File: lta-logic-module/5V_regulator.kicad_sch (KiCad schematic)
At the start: 0 parts

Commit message: Full sketch of logic module schematic.
- Add button inputs
- Add LED signal driver / PWM combination
- Add 5V regulator based on LM2592
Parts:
- added C? (x2): (no value), symbol Device:C_Polarized_Small_US
- added D?: (no value), symbol Device:D_Schottky
- added L?: (no value), symbol Device:L_Small
- added R?: (no value), symbol Device:R_Small
- added U?: (no value), symbol Regulator_Switching:LM2595T-5
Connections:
- new net: R?.2, U?.5 (~{ON}/OFF)
- new net GND: C?.2, C?.2, D?.2 (A), R?.1, U?.3 (GND)
- new net VBATT: C?.1, U?.2 (VIN)
- new net VDD: C?.1, L?.1, U?.4 (FB)
- new net VOUT: D?.1 (K), L?.2, U?.1 (OUT)
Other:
- note added: "5V0 Buck Regulator - 1A max current"
- note added: "8--28Vin, 24V typ"
- note added: "Estimated power budget ---------------- MCU -- 25.0mA Button LEDs -- 180.0mA 74LVC244A -- 0.1mA 4x 74LVC00A -- 0.2mA 2x 74LVC14A -- 0.1mA 3x PCF8574 -- 0.3mA Pull-ups -- 0.1mA 16x FET driver inputs -- 25.0mA ------- 231mA"
- note added: "MPN: EST227M035AG4AA 35V low-ESR aluminum I_RMS > 250mA"
- note added: "MPN: TPSD686M020R0150 AVX TPS 20V low-ESR tantalum"
- note added: "Regulated 5V0 output"
- note added: "Target design load is 300mA"

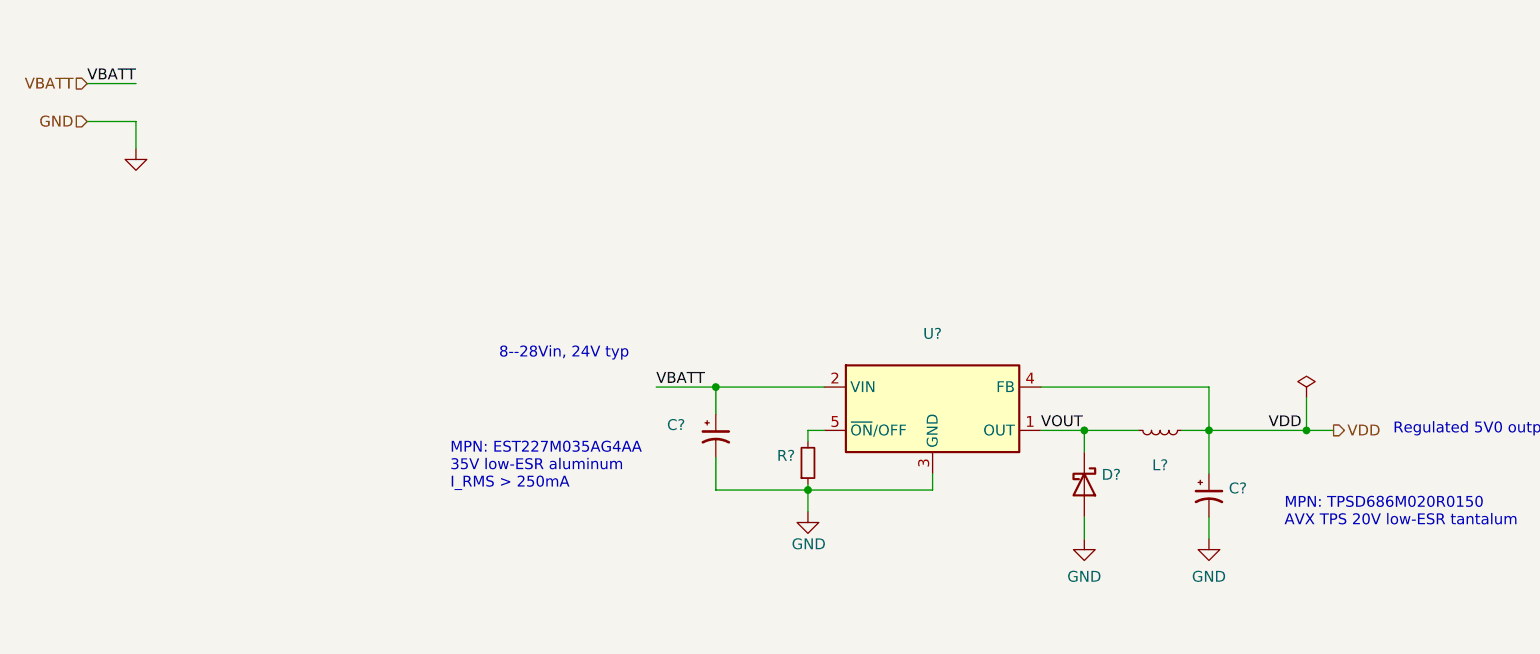
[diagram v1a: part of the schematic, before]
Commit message: Fix ERC violations.
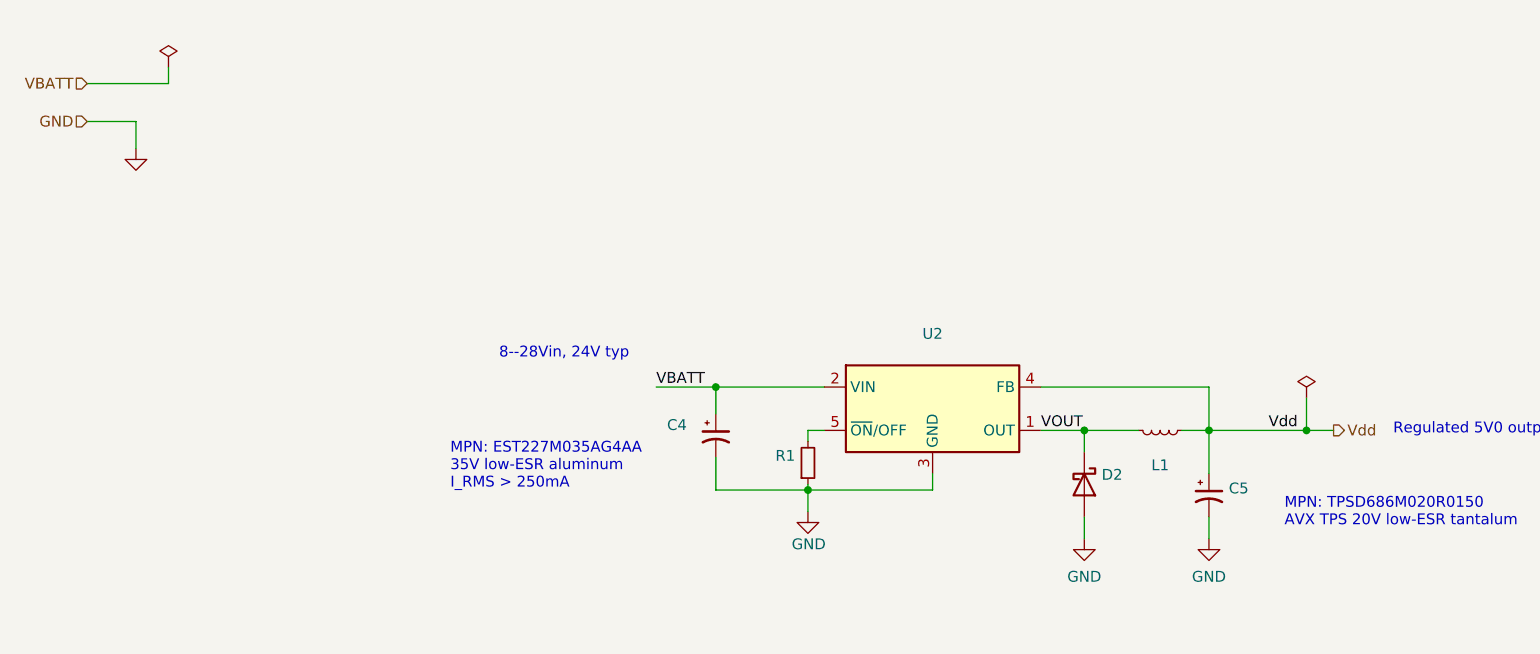
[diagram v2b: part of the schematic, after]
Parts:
- gave numbers to parts that had none: 6
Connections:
- net VDD renamed Vdd
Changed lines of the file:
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@@
+    (stroke (width 0) (type default) (color 0 0 0 0))
+  )
+  (wire (pts (xy 32.385 29.21) (xy 32.385 27.305))
     (stroke (width 0) (type default) (color 0 0 0 0))
   )
@@
     (stroke (width 0) (type default) (color 0 0 0 0))
   )
-  (wire (pts (xy 22.86 29.21) (xy 28.575 29.21))
+  (wire (pts (xy 22.86 29.21) (xy 32.385 29.21))
     (stroke (width 0) (type default) (color 0 0 0 0))
   )
@@
     (effects (font (size 1.27 1.27)) (justify left bottom))
   )
-  (label "VBATT" (at 28.575 29.21 180)
-    (effects (font (size 1.27 1.27)) (justify right bottom))
-  )
-  (label "VDD" (at 161.29 69.85 0)
+  (label "Vdd" (at 161.29 69.85 0)
     (effects (font (size 1.27 1.27)) (justify left bottom))
   )
@@
     (effects (font (size 1.27 1.27)) (justify right))
   )
-  (hierarchical_label "VDD" (shape output) (at 168.91 69.85 0)
+  (hierarchical_label "Vdd" (shape output) (at 168.91 69.85 0)
     (effects (font (size 1.27 1.27)) (justify left))
   )
   (symbol (lib_id "power:GND") (at 154.305 82.55 0) (unit 1)
     (in_bom yes) (on_board yes) (fields_autoplaced)
-    (property "Reference" "#PWR?" (id 0) (at 154.305 88.9 0)
+    (property "Reference" "#PWR020" (id 0) (at 154.305 88.9 0)
       (effects (font (size 1.27 1.27)) hide)
     )
@@
   (symbol (lib_id "Device:C_Polarized_Small_US") (at 96.52 70.485 0) (unit 1)
     (in_bom yes) (on_board yes)
-    (property "Reference" "C?" (id 0) (at 90.805 69.215 0)
+    (property "Reference" "C4" (id 0) (at 90.805 69.215 0)
       (effects (font (size 1.27 1.27)) (justify left))
     )
@@
   (symbol (lib_id "Device:R_Small") (at 107.315 73.66 0) (mirror x) (unit 1)
     (in_bom yes) (on_board yes) (fields_autoplaced)
-    (property "Reference" "R?" (id 0) (at 105.8165 72.8253 0)
+    (property "Reference" "R1" (id 0) (at 105.8165 72.8253 0)
       (effects (font (size 1.27 1.27)) (justify right))
     )
@@
   (symbol (lib_id "power:PWR_FLAG") (at 165.735 66.04 0) (unit 1)
     (in_bom yes) (on_board yes) (fields_autoplaced)
-    (property "Reference" "#FLG?" (id 0) (at 165.735 64.135 0)
+    (property "Reference" "#FLG03" (id 0) (at 165.735 64.135 0)
       (effects (font (size 1.27 1.27)) hide)
     )
@@
   (symbol (lib_id "Device:L_Small") (at 148.59 69.85 270) (unit 1)
     (in_bom yes) (on_board yes)
-    (property "Reference" "L?" (id 0) (at 148.59 73.9308 90))
+    (property "Reference" "L1" (id 0) (at 148.59 73.9308 90))
     (property "Value" "" (id 1) (at 148.59 71.755 90))
     (property "Footprint" "" (id 2) (at 148.59 69.85 0)
@@
   (symbol (lib_id "Device:D_Schottky") (at 139.7 76.2 270) (unit 1)
     (in_bom yes) (on_board yes) (fields_autoplaced)
-    (property "Reference" "D?" (id 0) (at 141.732 75.0478 90)
+    (property "Reference" "D2" (id 0) (at 141.732 75.0478 90)
       (effects (font (size 1.27 1.27)) (justify left))
     )
@@
   (symbol (lib_id "power:GND") (at 139.7 82.55 0) (unit 1)
     (in_bom yes) (on_board yes) (fields_autoplaced)
-    (property "Reference" "#PWR?" (id 0) (at 139.7 88.9 0)
+    (property "Reference" "#PWR019" (id 0) (at 139.7 88.9 0)
       (effects (font (size 1.27 1.27)) hide)
     )
@@
   (symbol (lib_id "power:GND") (at 28.575 36.83 0) (unit 1)
     (in_bom yes) (on_board yes) (fields_autoplaced)
-    (property "Reference" "#PWR?" (id 0) (at 28.575 43.18 0)
+    (property "Reference" "#PWR017" (id 0) (at 28.575 43.18 0)
       (effects (font (size 1.27 1.27)) hide)
     )
@@
   (symbol (lib_id "power:GND") (at 107.315 79.375 0) (unit 1)
     (in_bom yes) (on_board yes)
-    (property "Reference" "#PWR?" (id 0) (at 107.315 85.725 0)
+    (property "Reference" "#PWR018" (id 0) (at 107.315 85.725 0)
       (effects (font (size 1.27 1.27)) hide)
     )
@@
   (symbol (lib_id "Regulator_Switching:LM2595T-5") (at 121.92 67.31 0) (unit 1)
     (in_bom yes) (on_board yes) (fields_autoplaced)
-    (property "Reference" "U?" (id 0) (at 121.92 58.5302 0))
+    (property "Reference" "U2" (id 0) (at 121.92 58.5302 0))
     (property "Value" "" (id 1) (at 121.92 61.0671 0))
     (property "Footprint" "" (id 2) (at 123.19 73.66 0)
@@
   (symbol (lib_id "Device:C_Polarized_Small_US") (at 154.305 77.47 0) (unit 1)
     (in_bom yes) (on_board yes) (fields_autoplaced)
-    (property "Reference" "C?" (id 0) (at 156.6291 76.6416 0)
+    (property "Reference" "C5" (id 0) (at 156.6291 76.6416 0)
       (effects (font (size 1.27 1.27)) (justify left))
     )
@@
     (pin "2")
   )
+  (symbol (lib_id "power:PWR_FLAG") (at 32.385 27.305 0) (unit 1)
+    (in_bom yes) (on_board yes) (fields_autoplaced)
+    (property "Reference" "#FLG02" (id 0) (at 32.385 25.4 0)
+      (effects (font (size 1.27 1.27)) hide)
+    )
+    (property "Value" "" (id 1) (at 32.385 23.7292 0))
+    (property "Footprint" "" (id 2) (at 32.385 27.305 0)
+      (effects (font (size 1.27 1.27)) hide)
+    )
+    (property "Datasheet" "~" (id 3) (at 32.385 27.305 0)
+      (effects (font (size 1.27 1.27)) hide)
+    )
+    (pin "1")
+  )
 )

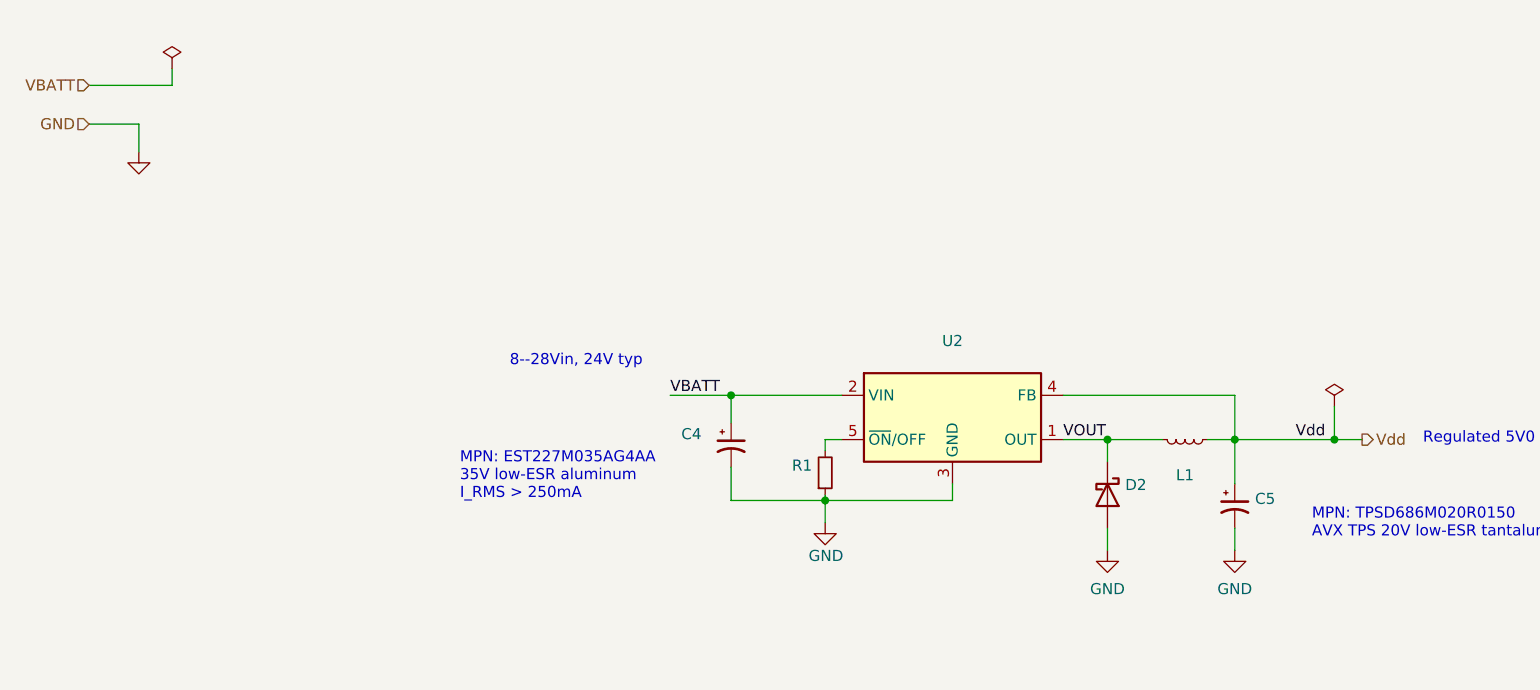
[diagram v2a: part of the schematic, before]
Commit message: Add TODOs, update some footprints.
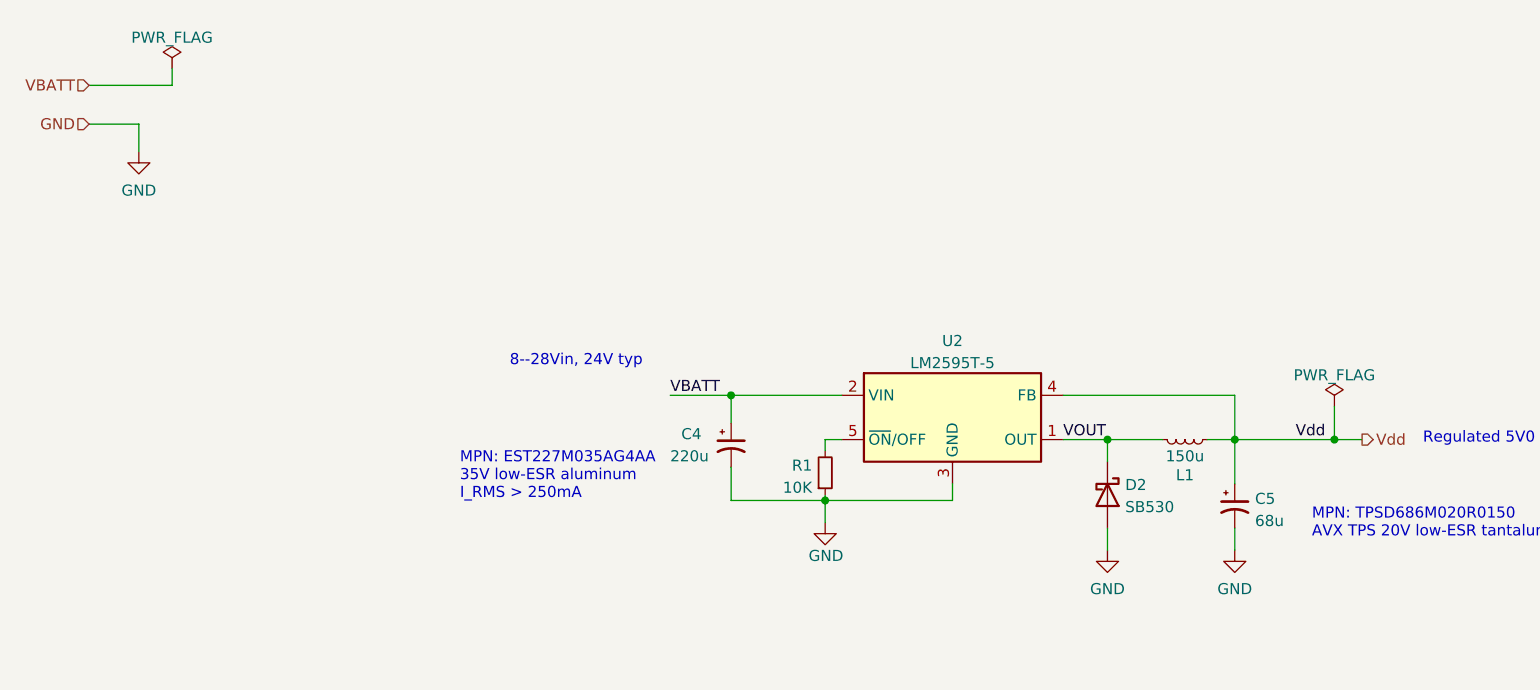
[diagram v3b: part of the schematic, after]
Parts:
- C4: value (none) -> 220u; footprint (none) -> Capacitor_THT:CP_Radial_D8.0mm_P3.50mm
- C5: value (none) -> 68u; footprint (none) -> Capacitor_Tantalum_SMD:CP_EIA-7343-30_AVX-N
- D2: value (none) -> SB530; footprint (none) -> Diode_THT:D_DO-201AD_P15.24mm_Horizontal
- L1: value (none) -> 150u; footprint (none) -> Aaron_THT:L_Radial_D13.5mm_P7.50mm
- R1: value (none) -> 10K; footprint (none) -> Resistor_SMD:R_0603_1608Metric; Comment (none) -> 10K 0603 resistor; +/-1%; 1/10W; MANUFACTURER (none) -> YAEGO; MPN (none) -> RC0603FR-0710KL
- U2: value (none) -> LM2595T-5; footprint (none) -> Package_TO_SOT_THT:TO-220-5_P3.4x3.7mm_StaggerOdd_Lead3.8mm_Vertical
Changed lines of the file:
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@@
       (effects (font (size 1.27 1.27)) (justify left))
     )
-    (property "Value" "" (id 1) (at 89.535 71.755 0)
-      (effects (font (size 1.27 1.27)) (justify left))
-    )
-    (property "Footprint" "" (id 2) (at 96.52 70.485 0)
+    (property "Value" "220u" (id 1) (at 89.535 71.755 0)
+      (effects (font (size 1.27 1.27)) (justify left))
+    )
+    (property "Footprint" "Capacitor_THT:CP_Radial_D8.0mm_P3.50mm" (id 2) (at 96.52 70.485 0)
       (effects (font (size 1.27 1.27)) hide)
     )
@@
       (effects (font (size 1.27 1.27)) (justify right))
     )
-    (property "Value" "" (id 1) (at 105.8165 75.3622 0)
+    (property "Value" "10K" (id 1) (at 105.8165 75.3622 0)
       (effects (font (size 1.27 1.27)) (justify right))
     )
-    (property "Footprint" "" (id 2) (at 107.315 73.66 0)
+    (property "Footprint" "Resistor_SMD:R_0603_1608Metric" (id 2) (at 107.315 73.66 0)
       (effects (font (size 1.27 1.27)) hide)
     )
@@
       (effects (font (size 1.27 1.27)) hide)
     )
+    (property "Comment" "10K 0603 resistor; +/-1%; 1/10W " (id 4) (at 107.315 73.66 0)
+      (effects (font (size 1.27 1.27)) hide)
+    )
+    (property "MANUFACTURER" "YAEGO" (id 5) (at 107.315 73.66 0)
+      (effects (font (size 1.27 1.27)) hide)
+    )
+    (property "MPN" "RC0603FR-0710KL" (id 6) (at 107.315 73.66 0)
+      (effects (font (size 1.27 1.27)) hide)
+    )
     (pin "1")
     (pin "2")
@@
       (effects (font (size 1.27 1.27)) hide)
     )
-    (property "Value" "" (id 1) (at 165.735 62.4642 0))
+    (property "Value" "PWR_FLAG" (id 1) (at 165.735 62.4642 0))
     (property "Footprint" "" (id 2) (at 165.735 66.04 0)
       (effects (font (size 1.27 1.27)) hide)
@@
     (in_bom yes) (on_board yes)
     (property "Reference" "L1" (id 0) (at 148.59 73.9308 90))
-    (property "Value" "" (id 1) (at 148.59 71.755 90))
-    (property "Footprint" "" (id 2) (at 148.59 69.85 0)
+    (property "Value" "150u" (id 1) (at 148.59 71.755 90))
+    (property "Footprint" "Aaron_THT:L_Radial_D13.5mm_P7.50mm" (id 2) (at 148.59 69.85 0)
       (effects (font (size 1.27 1.27)) hide)
     )
@@
       (effects (font (size 1.27 1.27)) (justify left))
     )
-    (property "Value" "" (id 1) (at 141.732 77.5847 90)
-      (effects (font (size 1.27 1.27)) (justify left))
-    )
-    (property "Footprint" "" (id 2) (at 139.7 76.2 0)
+    (property "Value" "SB530" (id 1) (at 141.732 77.5847 90)
+      (effects (font (size 1.27 1.27)) (justify left))
+    )
+    (property "Footprint" "Diode_THT:D_DO-201AD_P15.24mm_Horizontal" (id 2) (at 139.7 76.2 0)
       (effects (font (size 1.27 1.27)) hide)
     )
@@
       (effects (font (size 1.27 1.27)) hide)
     )
-    (property "Value" "" (id 1) (at 28.575 41.2734 0))
+    (property "Value" "GND" (id 1) (at 28.575 41.2734 0))
     (property "Footprint" "" (id 2) (at 28.575 36.83 0)
       (effects (font (size 1.27 1.27)) hide)
@@
     (in_bom yes) (on_board yes) (fields_autoplaced)
     (property "Reference" "U2" (id 0) (at 121.92 58.5302 0))
-    (property "Value" "" (id 1) (at 121.92 61.0671 0))
-    (property "Footprint" "" (id 2) (at 123.19 73.66 0)
+    (property "Value" "LM2595T-5" (id 1) (at 121.92 61.0671 0))
+    (property "Footprint" "Package_TO_SOT_THT:TO-220-5_P3.4x3.7mm_StaggerOdd_Lead3.8mm_Vertical" (id 2) (at 123.19 73.66 0)
       (effects (font (size 1.27 1.27) italic) (justify left) hide)
     )
@@
       (effects (font (size 1.27 1.27)) (justify left))
     )
-    (property "Value" "" (id 1) (at 156.6291 79.1785 0)
-      (effects (font (size 1.27 1.27)) (justify left))
-    )
-    (property "Footprint" "" (id 2) (at 154.305 77.47 0)
+    (property "Value" "68u" (id 1) (at 156.6291 79.1785 0)
+      (effects (font (size 1.27 1.27)) (justify left))
+    )
+    (property "Footprint" "Capacitor_Tantalum_SMD:CP_EIA-7343-30_AVX-N" (id 2) (at 154.305 77.47 0)
       (effects (font (size 1.27 1.27)) hide)
     )
@@
       (effects (font (size 1.27 1.27)) hide)
     )
-    (property "Value" "" (id 1) (at 32.385 23.7292 0))
+    (property "Value" "PWR_FLAG" (id 1) (at 32.385 23.7292 0))
     (property "Footprint" "" (id 2) (at 32.385 27.305 0)
       (effects (font (size 1.27 1.27)) hide)
